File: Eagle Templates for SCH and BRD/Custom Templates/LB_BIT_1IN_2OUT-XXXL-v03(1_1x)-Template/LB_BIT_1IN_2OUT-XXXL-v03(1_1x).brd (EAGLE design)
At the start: 21.5 x 71 mm, 21 parts, among them U1 LV321SOT23-5, U2 LV321SOT23-5, U3 LV321SOT23-5

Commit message: added bitlab logo and made minor changes to board templates. Updated littlebits library.
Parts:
- added U$2: (no value), LITTLEBITS:BITLAB-LOGO
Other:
- board text added: "iX Name Here"
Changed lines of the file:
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@@
 <layer number="113" name="extra" color="10" fill="1" visible="yes" active="yes"/>
 <layer number="116" name="Patch_BOT" color="9" fill="4" visible="yes" active="yes"/>
+<layer number="118" name="Rect_Pads" color="7" fill="1" visible="no" active="yes"/>
 <layer number="121" name="_tsilk" color="7" fill="1" visible="yes" active="yes"/>
 <layer number="122" name="_bsilk" color="7" fill="1" visible="yes" active="yes"/>
@@
 <wire x1="23.51" y1="74.65" x2="23.405" y2="74.65" width="0" layer="20"/>
 <text x="3.8" y="5.1" size="0.8128" layer="16" font="vector" ratio="12" rot="MR90">revX</text>
+<text x="21.8" y="39.63" size="1.3" layer="21" font="vector" rot="SR270" align="center">iX Name Here</text>
 </plain>
 <attributes>
@@
 <element name="U$3" library="LITTLEBITS" package="OSHWCREDIT" value="OSHWCREDIT" x="-86.66" y="-61.795"/>
 <element name="FRAME1" library="LITTLEBITS" package="FABDWG01-OHW" value="FRAME-LETTER" x="0" y="0"/>
+<element name="U$2" library="LITTLEBITS" package="BITLAB-LOGO" value="" x="20.2" y="43.9" rot="R270"/>
 </elements>
 <signals>

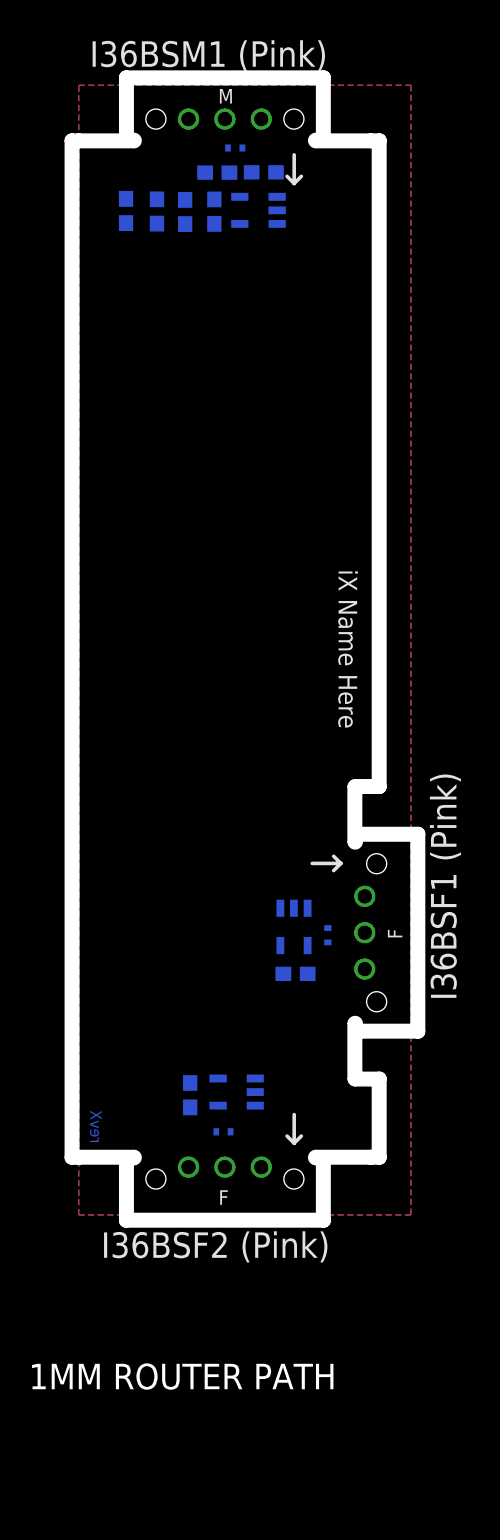
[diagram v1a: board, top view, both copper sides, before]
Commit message: Updated templates
- Added ferrite beads
- Moved text and annotations off of Nets layer
- Minor layout changes
- Removed I/O/W prefix from reference designators
- Removed output stage components from output bits
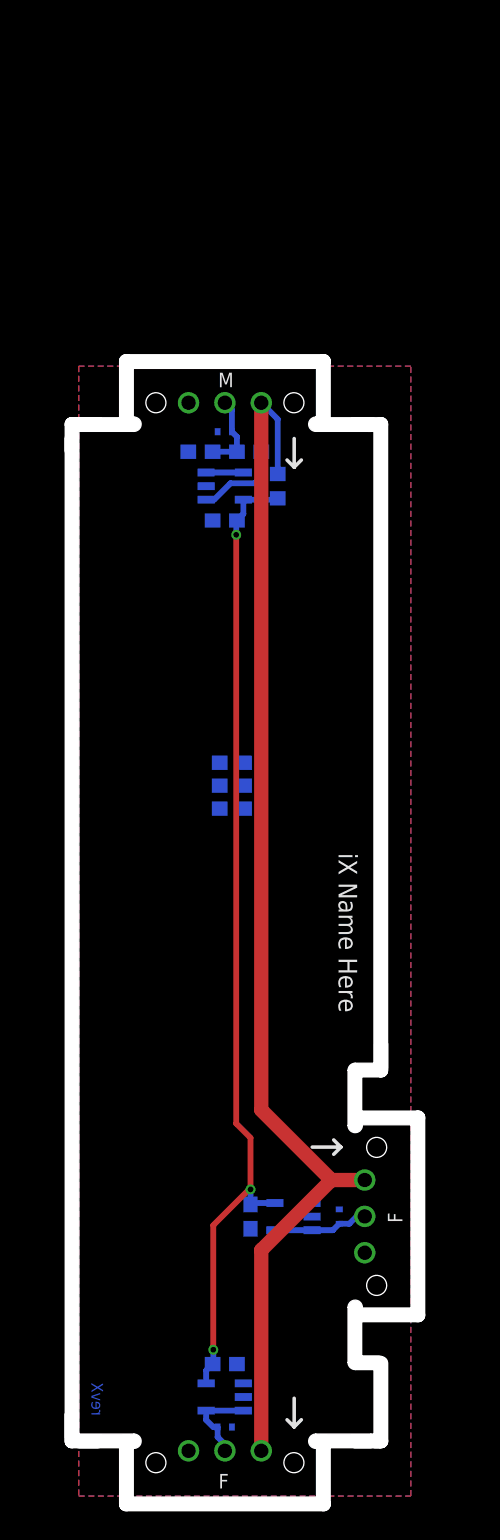
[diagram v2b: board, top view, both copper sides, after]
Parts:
- removed I36BSF1, I36BSF2: BITSNAP_V03_FEMALE, bitSnap:BITSNAP_V03_FEMALE
- removed I36BSM1: BITSNAP_V03_MALE, bitSnap:BITSNAP_V03_MALE
- removed I?C1: 0.1uF, LITTLEBITS:CAP-0603
- removed I?C2: 10uF, LITTLEBITS:CAP-0603
- removed I?C3, I?C4: 1.0uF, LITTLEBITS:CAP-0603
- removed I?R1: 1meg, LITTLEBITS:RES-0603
- removed I?R2: 10K, LITTLEBITS:RES-0603
- removed I?R3, I?R4: 3K3, LITTLEBITS:RES-0603
- removed I?TVS1, I?TVS2, I?TVS3: ESD9B5.0ST5G, LITTLEBITS:SOD-923
- removed U$17: (no value), ohw-logo:OSHW_FILLX150_NOTEXT
- added BSF1, BSF2: BITSNAP_V03_FEMALE, bitSnap:BITSNAP_V03_FEMALE
- added BSM1: BITSNAP_V03_MALE, bitSnap:BITSNAP_V03_MALE
- added C1: 0.1uF, LITTLEBITS:CAP-0603
- added C2: 10uF, LITTLEBITS:CAP-0603
- added C3, C4: 1.0uF, LITTLEBITS:CAP-0603
- added FB1: FERRITE-BEAD0603, LITTLEBITS:R0603
- added R3, R4: 3K3, LITTLEBITS:RES-0603
- added R5: 1meg, LITTLEBITS:RES-0603
- added R6: 10K, LITTLEBITS:RES-0603
- added TVS1, TVS2, TVS3: ESD9B5.0ST5G, LITTLEBITS:SOD-923
- added U$8: (no value), ohw-logo:OSHW_FILLX150_NOTEXT
- U$2: value (none) -> OSHWCREDIT; device LITTLEBITS:BITLAB-LOGO -> LITTLEBITS:OSHWCREDIT
- U$3: value OSHWCREDIT -> (none); device LITTLEBITS:OSHWCREDIT -> LITTLEBITS:BITLAB-LOGO
- moved U$2 148.3 mm to (-87.0, -58.5), turned to 0 degrees
- moved U$3 137.1 mm to (20.2, 24.1), turned to 270 degrees
- moved U1 70.3 mm to (18.0, -0.01)
- moved U3 31.2 mm to (13.2, 51.0), turned to 90 degrees
- moved U2 21.3 mm to (13.2, -12.6)
- moved U$1 7.46 mm to (-33.0, -65.6)
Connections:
- removed net N$4: I?R2.1, U1.1
- removed net SIG_OUT: I?TVS2.2, U2.3, U2.4
- removed net SIG_OUT1: I?TVS3.2, U3.3, U3.4
- new net LB_VCC: BSF1.VCC, BSF2.VCC, BSM1.VCC1, FB1.2
- new net N$5: R6.1, U3.1
- new net SIG1_OUT: BSF1.SIG, TVS2.2, U2.3, U2.4
- new net SIG2_OUT: BSF2.SIG, TVS1.2, U1.3, U1.4
- net GND: now also BSF1.GND, BSF2.GND, BSM1.GND1, C1.2, C2.2, C3.1, C4.1, R4.1, R5.1, TVS1.1, TVS2.1, TVS3.1; no longer I36BSF1.GND, I36BSF2.GND, I36BSM1.GND1, I?C1.2, I?C2.2, I?C3.1, I?C4.1, I?R1.1, I?R4.1, I?TVS1.1, I?TVS2.1, I?TVS3.1
- net N$1: now also U3.3, U3.4; no longer U3.1
- net N$2: now also U1.1; no longer U1.3, U1.4
- net SIG_IN: now also BSM1.SIG1, R5.2, R6.2, TVS3.2; no longer I36BSM1.SIG1, I?R1.2, I?R2.2, I?TVS1.2
- net VCC: now also C1.1, C3.2, C4.2, FB1.1, R3.2; no longer I36BSF1.VCC, I36BSF2.VCC, I36BSM1.VCC1, I?C1.1, I?C3.2, I?C4.2, I?R3.2
- net VREF: now also C2.1, R3.1, R4.2; no longer I?C2.1, I?R3.1, I?R4.2
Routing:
- net LB_VCC: track 0.00 -> 85.1 mm
- net VCC: track 0.00 -> 69.0 mm, vias 0 -> 3
- net SIG2_OUT: track 0.00 -> 6.68 mm
- net N$5: track 0.00 -> 6.26 mm
- net SIG1_OUT: track 0.00 -> 6.13 mm
- net SIG_IN: track 0.00 -> 5.47 mm
- net N$1: track 0.00 -> 2.60 mm
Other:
- board size 21.5 x 71 mm -> 21.6 x 71 mm
- board text removed: "1MM ROUTER PATH"
- board text removed: "I36BSF1 (Pink)"
- board text removed: "I36BSF2 (Pink)"
- board text removed: "I36BSM1 (Pink)"
